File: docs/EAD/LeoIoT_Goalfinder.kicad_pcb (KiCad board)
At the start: 2 copper layers, 100 x 50 mm, 17 parts, among them J1 USB_B_Micro_Breakout, J2 LED Strip, J3 GAIN, Q1 IRFZ44N, U1 ESP32_D1_mini, U2 VL53L0X_Breakout, U3 MAX98357A_Breakout, U4 SW420_Breakout

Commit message: updated PCB layout (extended wire width)
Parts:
- moved REF** 0.31 mm to (197.2, 90.2)
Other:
- outline, holes or cut-outs redrawn

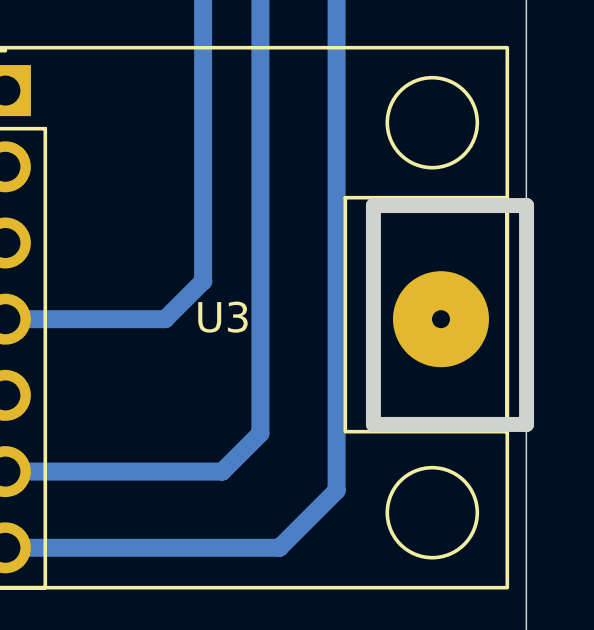
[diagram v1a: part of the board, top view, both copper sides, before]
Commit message: finished PCB introduced housing
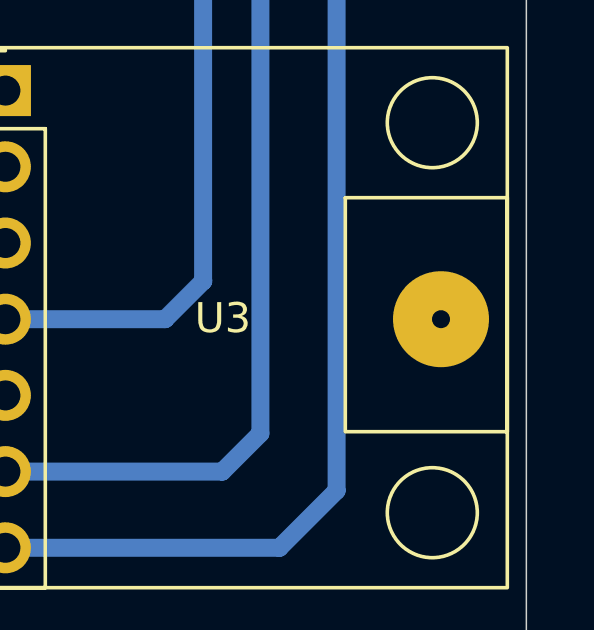
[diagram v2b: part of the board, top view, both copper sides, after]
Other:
- outline, holes or cut-outs redrawn
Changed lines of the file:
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@@
 			)
 		)
-		(sheetname "Stammblatt")
-		(sheetfile "LeoIoT_Goalfinder.kicad_sch")
 		(attr through_hole)
 		(fp_line
@@
 		(model "${SITOHOME_3DMODELS}/Mono_Enclosed_Speaker_3W-4Ohm.stp"
 			(offset
-				(xyz 35 -15 0)
+				(xyz 35 -15 4)
 			)
 			(scale
@@
 			)
 		)
+	)
+	(gr_rect
+		(start 100 60)
+		(end 200 110)
+		(stroke
+			(width 0.05)
+			(type default)
+		)
+		(fill none)
+		(layer "Edge.Cuts")
 	)
 	(gr_rect
@@
 		)
 		(fill none)
-		(layer "Edge.Cuts")
-	)
-	(gr_rect
-		(start 100 60)
-		(end 200 110)
-		(stroke
-			(width 0.05)
-			(type default)
-		)
-		(fill none)
-		(layer "Edge.Cuts")
+		(layer "User.5")
 	)
 	(gr_text "HTL Leonding 2024"

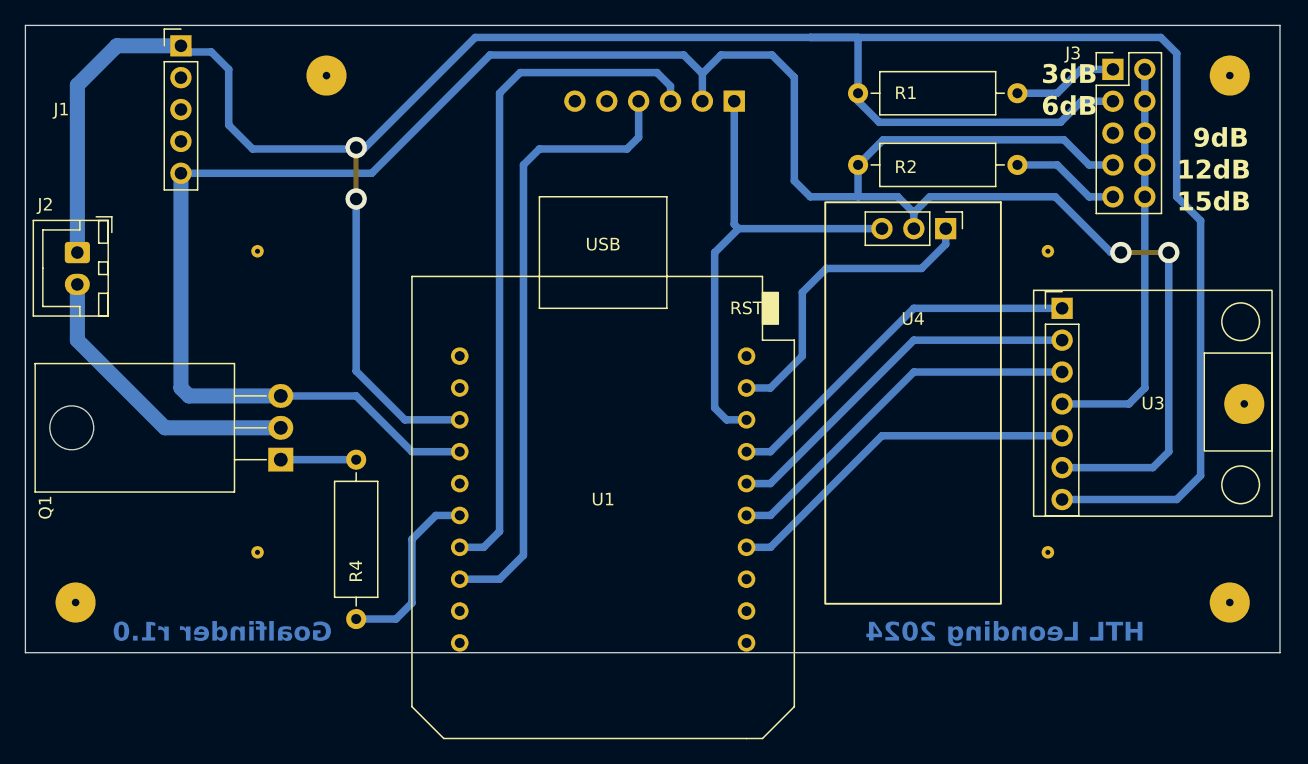
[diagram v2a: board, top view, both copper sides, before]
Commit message: added power support capacities, updated schematic and PCB to r1.1
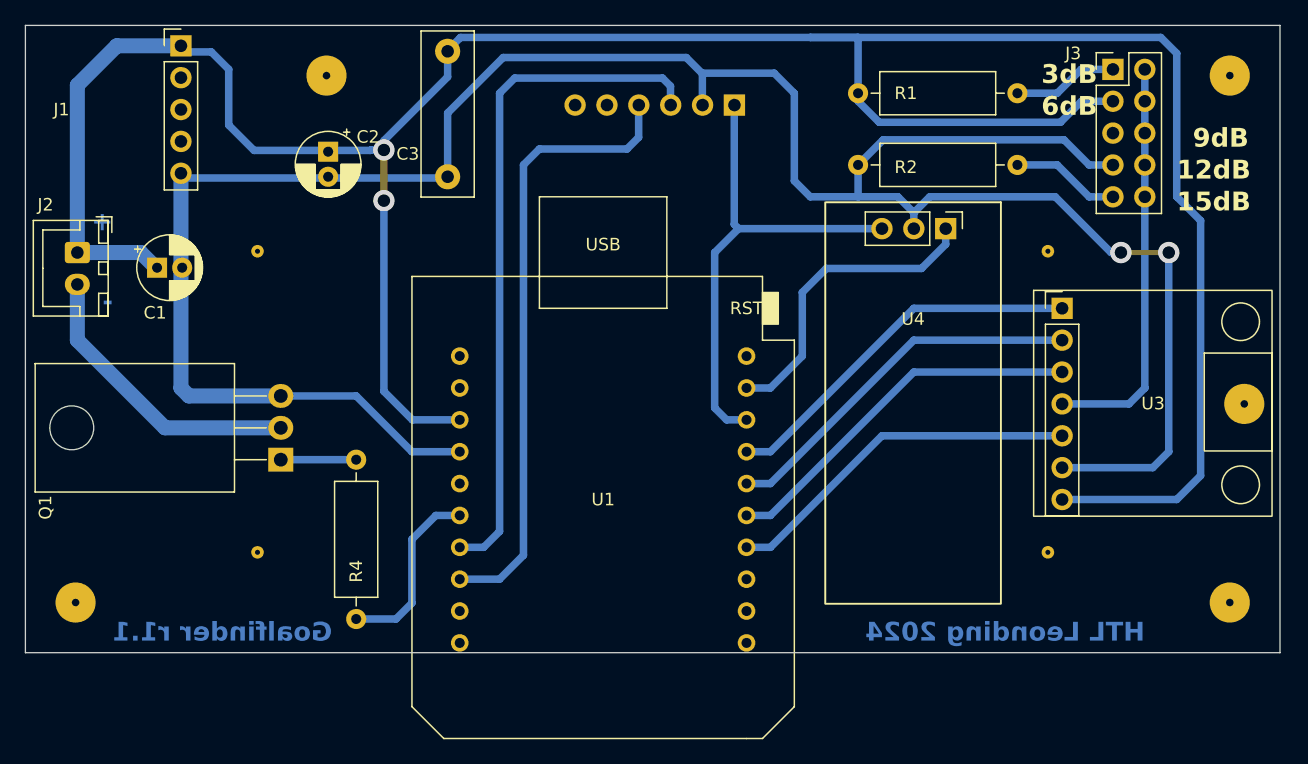
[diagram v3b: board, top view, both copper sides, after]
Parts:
- added C1: 22µF, Capacitor_THT:CP_Radial_D5.0mm_P2.00mm, F.Cu at (110.5, 79.3)
- added C2: 4,7µF, Capacitor_THT:CP_Radial_D5.0mm_P2.00mm, F.Cu at (124.1, 70.1)
- added C3: 0,1µF, Capacitor_THT:C_Rect_L13.0mm_W4.0mm_P10.00mm_FKS3_FKP3_MKS4, F.Cu at (133.7, 62.1)
- moved U2 0.31 mm to (156.5, 66.3)
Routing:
- net 5V: track 217.0 -> 224.1 mm
- net GND: track 190.6 -> 191.7 mm
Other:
- board text added: "+"
- board text added: "-"
- board text added: "Goalfinder r1.1"
- board text removed: "Goalfinder r1.0"

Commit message: improved HW: - added capacitors for each breakout board - made GND lines wider and added GND shield areas - added HW revision 01.02 added technical drawings for case factoring
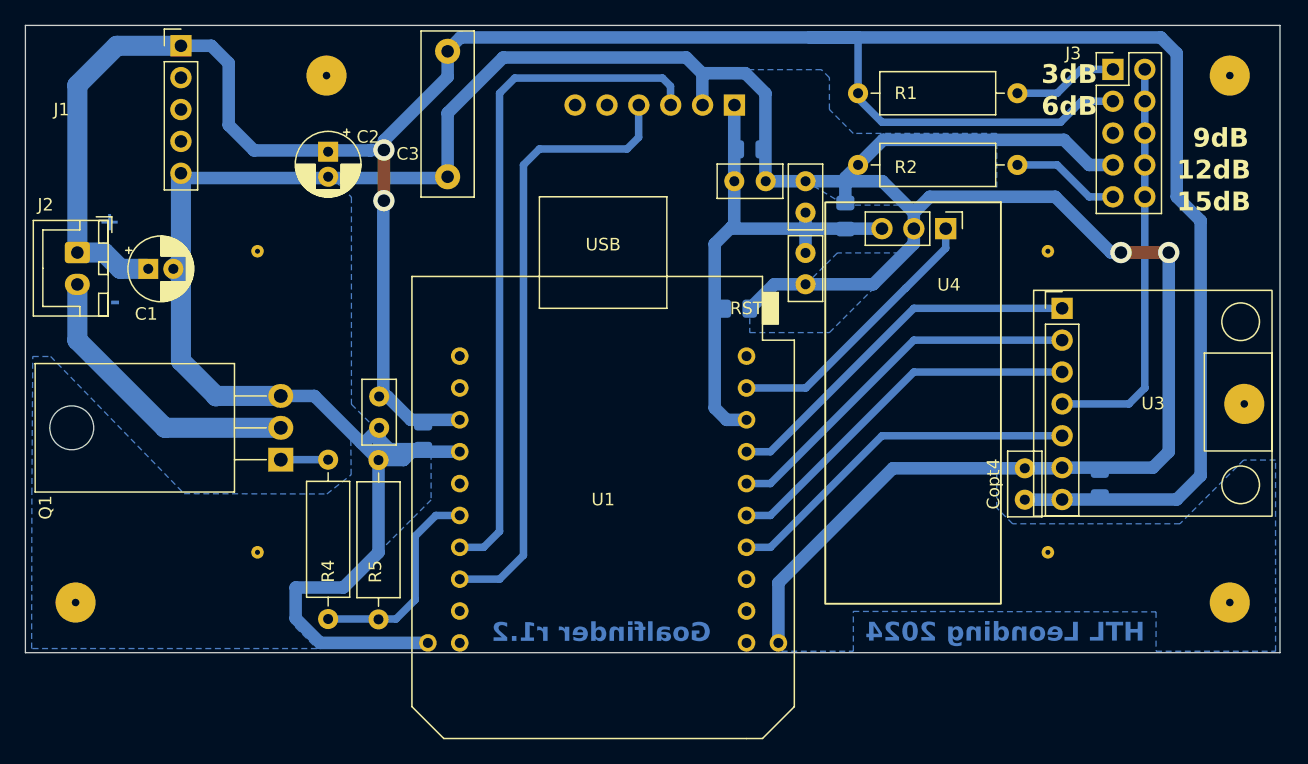
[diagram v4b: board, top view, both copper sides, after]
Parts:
- added C4: 100nF, Capacitor_SMD:C_0805_2012Metric_Pad1.18x1.45mm_HandSolder, B.Cu at (185.6, 96.5)
- added C5: 100nF, Capacitor_SMD:C_0805_2012Metric_Pad1.18x1.45mm_HandSolder, B.Cu at (165.4, 75.2)
- added C6: 100nF, Capacitor_SMD:C_0805_2012Metric_Pad1.18x1.45mm_HandSolder, B.Cu at (157.7, 69.9)
- added C7: 100nF, Capacitor_SMD:C_0805_2012Metric_Pad1.18x1.45mm_HandSolder, B.Cu at (131.7, 92.7)
- added C8: 100nF, Capacitor_SMD:C_0805_2012Metric_Pad1.18x1.45mm_HandSolder, B.Cu at (156.7, 82.6)
- added Copt4: 100nF, Capacitor_THT:C_Disc_D5.0mm_W2.5mm_P2.50mm, F.Cu at (179.7, 97.8)
- added Copt5: 100nF, Capacitor_THT:C_Disc_D5.0mm_W2.5mm_P2.50mm, F.Cu at (162.2, 74.9)
- added Copt6: 100nF, Capacitor_THT:C_Disc_D5.0mm_W2.5mm_P2.50mm, F.Cu at (156.5, 72.4)
- added Copt7: 100nF, Capacitor_THT:C_Disc_D5.0mm_W2.5mm_P2.50mm, F.Cu at (128.2, 89.6)
- added Copt8: 100nF, Capacitor_THT:C_Disc_D5.0mm_W2.5mm_P2.50mm, F.Cu at (162.2, 78.1)
- added R5: 33k, Resistor_THT:R_Axial_DIN0309_L9.0mm_D3.2mm_P12.70mm_Horizontal, F.Cu at (128.1, 107.3)
- moved R4 2.23 mm to (124.1, 107.3)
- moved C1 0.71 mm to (109.8, 79.4)
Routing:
- net GND: track 191.7 -> 278.1 mm
- net 3V3: track 39.7 -> 43.3 mm
- net Net-(U1-IO_13/TCK): track 24.8 -> 22.0 mm
- net 5V: track 224.1 -> 226.9 mm
- net Net-(U1-IO_17/U2_TXC): track 14.7 -> 16.9 mm
- net Net-(Q1-G): track 6.01 -> 3.77 mm
- added copper zone on B.Cu, net GND
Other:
- board text added: "Goalfinder r1.2"
- board text removed: "Goalfinder r1.1"
